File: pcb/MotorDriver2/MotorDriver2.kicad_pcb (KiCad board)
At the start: 4 copper layers, 112 parts, among them IC1 STM32C092RCT6, J1 GT-USB-7010ASV, J2 Conn_01x02, J3 Conn_01x02, J4 Conn_01x02, J5 Conn_01x02, Q1 IRLZ44NSTRLPBF, Q2 IRLZ44NSTRLPBF, Q3 IRLZ44NSTRLPBF, Q4 IRLZ44NSTRLPBF, Q5 IRLZ44NSTRLPBF, Q6 IRLZ44NSTRLPBF, Q7 IRLZ44NSTRLPBF, Q8 IRLZ44NSTRLPBF, SW1 K2-6639SP-C4SC-04, SW2 K2-6639SP-C4SC-04, SW3 K2-6639SP-C4SC-04, U1 NCP361SNT1G, U2 CH340X, U3 XIAO-ESP32-C5-DIP, U4 MCP2562FDT-H/SN, U5 MCP2562FDT-H/SN, U6 LM324DR, Y1 48 MHz, Y2 32.768 kHz

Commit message: Laying out PCB
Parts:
- removed H1, H2, H3: MountingHole, MountingHole:ToolingHole_1.152mm
- added C22: 100 nF, Capacitor_SMD:C_0603_1608Metric, F.Cu at (160.5, 145.5)
- added C23: 100 nF, Capacitor_SMD:C_0603_1608Metric, F.Cu at (160.5, 149.5)
- added C25: 4.7 uF, Capacitor_SMD:C_0603_1608Metric, F.Cu at (133.0, 115.5)
- added C26: 100 nF, Capacitor_SMD:C_0402_1005Metric, F.Cu at (133.5, 114.0)
- added D12: SM5819L2-TP, CapstoneFootprints:SDO_SM5819L2-TP_MCE, F.Cu at (181.5, 118.2)
- added D13: SM5819L2-TP, CapstoneFootprints:SDO_SM5819L2-TP_MCE, F.Cu at (181.5, 87.8)
- added D14: SM5819L2-TP, CapstoneFootprints:SDO_SM5819L2-TP_MCE, F.Cu at (122.2, 56.0)
- added IC2: CP2102N-A02-GQFN20R, CapstoneFootprints:CP2102NA02GQFN20, F.Cu at (135.5, 110.8)
- added R34: 10k, Resistor_SMD:R_0402_1005Metric, F.Cu at (139.5, 112.5)
- added R35: 1.5k, 1%, Resistor_SMD:R_0402_1005Metric, F.Cu at (126.0, 112.5)
- added R36: 1k, Resistor_SMD:R_0402_1005Metric, F.Cu at (136.0, 106.5)
- added R37: 1k, Resistor_SMD:R_0402_1005Metric, F.Cu at (132.5, 105.5)
- added R38: 10k, Resistor_SMD:R_0402_1005Metric, F.Cu at (218.5, 120.5)
- added R39: 1, Resistor_SMD:R_1206_3216Metric, F.Cu at (165.2, 101.5)
- added R40: 1, Resistor_SMD:R_1206_3216Metric, F.Cu at (165.2, 123.8)
- added R41: 10k, Resistor_SMD:R_0402_1005Metric, F.Cu at (236.0, 91.0)
- added R42: 10k, Resistor_SMD:R_0402_1005Metric, F.Cu at (236.0, 95.7)
- added R43: 1, Resistor_SMD:R_1206_3216Metric, F.Cu at (165.2, 83.8)
- added R44: 1, Resistor_SMD:R_1206_3216Metric, F.Cu at (122.5, 77.0)
- added TP1: TestPoint, TestPoint:TestPoint_Pad_1.0x1.0mm, B.Cu at (160.5, 91.5)
- added TP2: TestPoint, TestPoint:TestPoint_Pad_1.0x1.0mm, B.Cu at (160.5, 93.5)
- added TP3: TestPoint, TestPoint:TestPoint_Pad_1.0x1.0mm, B.Cu at (160.5, 95.5)
- C1, C2: value MAL214297108E3 -> Honor Elec RVT1H470M0607; footprint footprintLib:CAPAE680X800N -> CapstoneFootprints:CAPAE680X800N
- C10: value 100 nF -> Honor Elec RVT1H470M0607; footprint Capacitor_SMD:C_0402_1005Metric -> CapstoneFootprints:CAPAE680X800N
- C11: value 10 nF -> Honor Elec RVT1H470M0607; footprint Capacitor_SMD:C_0402_1005Metric -> CapstoneFootprints:CAPAE680X800N
- C12: value 100 nF -> 100 pF
- C20, C21: value MAL214297108E3 -> 100 nF; footprint footprintLib:CAPAE680X800N -> Capacitor_SMD:C_0603_1608Metric
- Conn2, Conn4, Conn5, Conn6, Conn8, R5, R7: moved to B.Cu
- D1: value SM5819L2-TP -> SP0502BAHTG; footprint footprintLib:SDO_SM5819L2-TP_MCE -> CapstoneFootprints:SOT95P237X112-3N
- D10, D9: value SM5819L2-TP -> LED; footprint footprintLib:SDO_SM5819L2-TP_MCE -> Diode_SMD:D_0402_1005Metric
- D11, D2, D3, D4, D8: footprint footprintLib:SDO_SM5819L2-TP_MCE -> CapstoneFootprints:SDO_SM5819L2-TP_MCE
- IC1: footprint footprintLib:QFP50P1200X1200X160-64N -> CapstoneFootprints:QFP50P1200X1200X160-64N
- J1: footprint footprintLib:USB4110-GF-A_GCT -> CapstoneFootprints:USB4110-GF-A_GCT
- Q1, Q3, Q5, Q6: footprint footprintLib:NMOSGDS_D2PAK_INF -> CapstoneFootprints:NMOSGDS_D2PAK_INF
- Q2, Q4, Q7, Q8: footprint footprintLib:NMOSGDS_D2PAK_INF -> CapstoneFootprints:NMOSGDS_D2PAK_INF; moved to B.Cu
- R13, R14: value 10k -> 20k
- R24, R25: value 1 -> 20k; footprint Resistor_SMD:R_1206_3216Metric -> Resistor_SMD:R_0402_1005Metric
- R26: value 10k -> 1k
- R27: value 10k -> 47.5k
- R28: value 1 -> 22.1k; footprint Resistor_SMD:R_1206_3216Metric -> Resistor_SMD:R_0402_1005Metric
- R29: value 1 -> 10k; footprint Resistor_SMD:R_1206_3216Metric -> Resistor_SMD:R_0402_1005Metric
- SW1, SW2, SW3: footprint footprintLib:K2-6639SP-C4SC-04 -> CapstoneFootprints:K2-6639SP-C4SC-04
- U1: footprint footprintLib:SOT95P275X110-5N -> CapstoneFootprints:SOT95P275X110-5N
- U2: value CH340X -> MAX40200AUK; footprint Package_SO:MSOP-10_3x3mm_P0.5mm -> Package_TO_SOT_SMD:SOT-23-5
- U3: footprint footprintLib:XIAO-ESP32-C5-DIP -> CapstoneFootprints:XIAO-ESP32-C5-DIP
- U6: footprint footprintLib:D14 -> CapstoneFootprints:D14
- VR1, VR2, VR3, VR4: footprint footprintLib:TS53YJ105MR10 -> CapstoneFootprints:TS53YJ105MR10
- Y1: footprint footprintLib:ECS-480-8-30-JGN-TR -> CapstoneFootprints:ECS-480-8-30-JGN-TR
- Y2: footprint footprintLib:MU00527-32.768K -> CapstoneFootprints:MU00527-32.768K
- moved Conn5 105.9 mm to (184.5, 96.0)
- moved Conn6 99.8 mm to (184.5, 86.5), turned to 180 degrees
- moved D11 84.8 mm to (181.5, 97.0), turned to -90 degrees
- moved Q7 84.8 mm to (173.0, 88.6), turned to 90 degrees
- moved Q6 84.3 mm to (173.1, 118.2), turned to -90 degrees
- moved R24 84.0 mm to (153.5, 142.0), turned to 180 degrees
- moved Q1 82.7 mm to (173.0, 96.5), turned to -90 degrees
- moved R25 77.5 mm to (153.8, 146.2), turned to 180 degrees
- moved C20 77.0 mm to (160.5, 137.0), turned to 180 degrees
- moved R14 74.2 mm to (154.0, 151.0), turned to 0 degrees
- moved C21 70.7 mm to (160.5, 141.0), turned to 180 degrees
- moved R13 66.6 mm to (165.4, 92.2), turned to 0 degrees
- moved R26 66.1 mm to (138.5, 114.5), turned to 0 degrees
- moved Conn7 66.0 mm to (129.2, 53.0), turned to 90 degrees
- moved D10 65.1 mm to (132.5, 107.0), turned to 180 degrees
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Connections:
- net /FDCAN/CAN_N renamed /digiControls/CAN_N
- net /FDCAN/CAN_P renamed /digiControls/CAN_P
- net /motorDriver_Pads12/Motor2- renamed /motors1/Motor1b-
- net /motorDriver_Pads12/Motor4- renamed /motors1/Motor2b-
- C10 pad 1: GND -> 5V
- C10 pad 2: 3V3 -> GND
- C11 pad 1: Net-(U2-V3) -> 5V
- C20 pad 1: 5V -> GND
- C20 pad 2: GND -> SensorAFilt
- C21 pad 1: 5V -> GND
- C21 pad 2: GND -> SensorBFilt
- Conn1 pad 2: /motorDriver_Pads12/Motor1- -> /motors1/Motor1a-
- Conn3 pad 2: /motorDriver_Pads12/Motor3- -> /motors1/Motor2a-
- Conn5 pad 2: /motorDriver_Pads34/Motor5- -> /motors2/Motor3a-
- Conn6 pad 2: /motorDriver_Pads34/Motor6- -> /motors2/Motor3b-
- Conn7 pad 2: /motorDriver_Pads34/Motor7- -> /motors2/Motor4a-
- Conn8 pad 2: /motorDriver_Pads34/Motor8- -> /motors2/Motor4b-
- D1 pad 1: 5V -> USB_D-
- D1 pad 2: /motorDriver_Pads34/Motor5- -> USB_D+
- D10 pad 1: 5V -> Net-(D10-K)
- D10 pad 2: /motorDriver_Pads34/Motor6- -> Net-(D10-A)
- D11 pad 2: /motorDriver_Pads34/Motor8- -> /motors2/Motor3a-
- D3 pad 2: /motorDriver_Pads12/Motor3- -> /motors1/Motor1a-
- D8 pad 2: /motorDriver_Pads12/Motor1- -> /motors2/Motor4a-
- D9 pad 1: 5V -> Net-(D9-K)
- D9 pad 2: /motorDriver_Pads34/Motor7- -> Net-(D9-A)
- IC1 pad 17: !CTS -> !CTS_STM
- IC1 pad 18: !RTS -> !RTS_STM
- IC1 pad 21: SensorAOut -> SensorAFilt
- IC1 pad 24: Motor4_PWM -> unconnected-(IC1-PA7-Pad24)
- IC1 pad 25: unconnected-(IC1-PC4-Pad25) -> Motor2a_PWM
- IC1 pad 26: unconnected-(IC1-PC5-Pad26) -> Motor2b_PWM
- IC1 pad 27: SensorDOut -> unconnected-(IC1-PB0-Pad27)
- IC1 pad 28: unconnected-(IC1-PB1-Pad28) -> SensorBFilt
- IC1 pad 30: unconnected-(IC1-PB10-Pad30) -> SensorCFilt
- IC1 pad 32: unconnected-(IC1-PB12-Pad32) -> SensorDFilt
- IC1 pad 38: unconnected-(IC1-PC6-Pad38) -> Motor3b_PWM
- IC1 pad 39: unconnected-(IC1-PC7-Pad39) -> Motor3a_PWM
- IC1 pad 40: unconnected-(IC1-PD8-Pad40) -> /stm32/SPI1_SCK
- IC1 pad 43: unconnected-(IC1-PA11_[PA9]-Pad43) -> /stm32/SPI1_MISO
- IC1 pad 44: unconnected-(IC1-PA12_[PA10]-Pad44) -> /stm32/SPI1_MOSI
- IC1 pad 47: Motor3_PWM -> Motor1a_PWM
- IC1 pad 57: Motor2_PWM -> Motor1b_PWM
- IC1 pad 58: Motor1_PWM -> unconnected-(IC1-PB4-Pad58)
- IC1 pad 60: unconnected-(IC1-PB6-Pad60) -> Motor4a_PWM
- IC1 pad 61: unconnected-(IC1-PB7-Pad61) -> Motor4b_PWM
- Q1 pad 1: Motor1_PWM -> Motor3a_PWM
- Q1 pad 2: /motorDriver_Pads34/Motor5- -> /motors2/Motor3a-
- Q2 pad 1: Motor2_PWM -> Motor1b_PWM
- Q3 pad 1: Motor3_PWM -> Motor1a_PWM
- Q3 pad 2: /motorDriver_Pads12/Motor3- -> /motors1/Motor1a-
- Q4 pad 1: Motor4_PWM -> Motor2b_PWM
- Q5 pad 1: Motor1_PWM -> Motor4a_PWM
- Q5 pad 2: /motorDriver_Pads12/Motor1- -> /motors2/Motor4a-
- Q6 pad 1: Motor3_PWM -> Motor2a_PWM
- Q6 pad 2: /motorDriver_Pads34/Motor7- -> /motors1/Motor2a-
- Q7 pad 1: Motor2_PWM -> Motor3b_PWM
- Q7 pad 2: /motorDriver_Pads34/Motor6- -> /motors2/Motor3b-
- Q8 pad 1: Motor4_PWM -> Motor4b_PWM
- Q8 pad 2: /motorDriver_Pads34/Motor8- -> /motors2/Motor4b-
- R1 pad 1: Motor1_PWM -> Motor4a_PWM
- R10 pad 1: !DTR -> (no net)
- R10 pad 2: BOOT -> (no net)
- R13 pad 1: Motor1_PWM -> SensorAOut
- R13 pad 2: GND -> SensorAFilt
- R14 pad 1: Motor3_PWM -> SensorBOut
- R14 pad 2: GND -> SensorBFilt
- R2 pad 1: Motor3_PWM -> Motor1a_PWM
- R24 pad 1: Net-(Q1-S) -> SensorDOut
- R24 pad 2: GND -> SensorDFilt
- R25 pad 1: Net-(Q6-S) -> SensorCOut
- R25 pad 2: GND -> SensorCFilt
- R26 pad 1: Motor2_PWM -> Net-(IC2-RSTB)
- R26 pad 2: GND -> 3V3
- R27 pad 1: Motor4_PWM -> Net-(IC2-VBUS)
- R28 pad 1: Net-(Q7-S) -> Net-(IC2-VBUS)
- R28 pad 2: GND -> 5V_USB
- R29 pad 1: Net-(Q8-S) -> Motor3a_PWM
- R5 pad 1: Motor2_PWM -> Motor1b_PWM
- R6 pad 1: Motor4_PWM -> Motor2b_PWM
- U2 pad 1: USB_D+ -> 5V
- U2 pad 2: USB_D- -> GND
- U2 pad 3: GND -> 5V
- U2 pad 4: !RTS -> unconnected-(U2-NC-Pad4)
- U2 pad 5: !CTS -> Net-(U2-OUT)
- U3 pad 14: 5V -> Net-(U2-OUT)
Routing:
- net 5V: track 259.9 -> 63.8 mm
- net Motor1_PWM: track 34.2 -> 0.00 mm
- net Motor4b_PWM: track 0.00 -> 33.2 mm, vias 0 -> 1
- net Motor4a_PWM: track 0.00 -> 29.7 mm
- net Motor4_PWM: track 26.1 -> 0.00 mm, vias 2 -> 0
- net Motor2_PWM: track 22.2 -> 0.00 mm, vias 2 -> 0
- net 3V3: track 42.3 -> 24.2 mm, vias 9 -> 4
- net !RTS: track 17.8 -> 0.00 mm, vias 2 -> 0
- net !CTS: track 16.1 -> 0.00 mm, vias 2 -> 0
- net /motorDriver_Pads34/Motor7-: track 15.1 -> 0.00 mm
- net BOOT: track 16.9 -> 1.97 mm
- net USER_BTN: track 19.1 -> 4.89 mm
- net SensorBIn: track 6.87 -> 20.9 mm
- net SensorAIn: track 15.5 -> 29.5 mm, vias 0 -> 2
- net NRST: track 24.9 -> 10.9 mm
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- removed copper zone on B.Cu, net GND
- removed copper zone on F.Cu, net GND
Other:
- board outline added: 76.5 x 82 mm
- board text added: "Emma Ouyang, Emma Steinberg Ashley Luo, Siyang Sun"
- board text removed: "Emma Ouyang, Emma Steinberg, Ashley Luo, Siyang Sun"
- board text removed: "WARNING: DO NOT USE ESP USB IF BATTERY IS ON"

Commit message: Finished pcb layout
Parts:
- removed D1: SP0502BAHTG, CapstoneFootprints:SOT95P237X112-3N
- removed R10: DNP, Resistor_SMD:R_0402_1005Metric
- added G***: LOGO, LOGO, F.Cu at (117.0, 127.0)
- added U7: USBLC6-2SC6, Package_TO_SOT_SMD:SOT-23-6, F.Cu at (128.5, 111.0)
- C20, C21, C22, C23: footprint Capacitor_SMD:C_0603_1608Metric -> Capacitor_SMD:C_0402_1005Metric
- J1: value GT-USB-7010ASV -> USB4110-GF-A
- R5, R7: moved to F.Cu
- moved R42 111.6 mm to (126.0, 77.0), turned to -90 degrees
- moved R41 71.0 mm to (165.0, 92.5), turned to 180 degrees
- moved R38 56.7 mm to (162.0, 116.0), turned to -90 degrees
- moved C23 46.3 mm to (152.0, 104.0)
- moved R14 44.7 mm to (149.8, 106.5)
- moved C22 40.9 mm to (155.0, 105.0)
- moved R25 40.3 mm to (153.0, 106.0), turned to 90 degrees
- moved C21 36.7 mm to (151.3, 105.5)
- moved R24 35.5 mm to (154.5, 106.5), turned to 90 degrees
- moved C20 33.6 mm to (148.8, 105.5)
- moved R13 22.7 mm to (147.8, 106.5), turned to 180 degrees
- moved R11 10.6 mm to (126.0, 97.0), turned to -90 degrees
- moved R2 10.3 mm to (162.0, 74.5), turned to 90 degrees
- moved D7 8.73 mm to (124.5, 97.0), turned to -90 degrees
- moved G*** 8.06 mm to (124.0, 127.0)
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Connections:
- IC1 pad 22: unconnected-(IC1-PA5-Pad22) -> SensorBFilt
- IC1 pad 23: unconnected-(IC1-PA6-Pad23) -> SensorCFilt
- IC1 pad 24: unconnected-(IC1-PA7-Pad24) -> SensorDFilt
- IC1 pad 28: SensorBFilt -> unconnected-(IC1-PB1-Pad28)
- IC1 pad 30: SensorCFilt -> unconnected-(IC1-PB10-Pad30)
- IC1 pad 32: SensorDFilt -> unconnected-(IC1-PB12-Pad32)
- R28 pad 2: 5V_USB -> VBUS
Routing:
- net GND: track 18.1 -> 99.3 mm, vias 11 -> 60
- net 5V: track 63.8 -> 102.9 mm, vias 5 -> 6
- net BOOT: track 1.97 -> 38.2 mm, vias 0 -> 2
- net 3V3: track 24.2 -> 60.2 mm, vias 4 -> 16
- net VBUS: track 9.72 -> 34.7 mm, vias 0 -> 2
- net Motor1b_PWM: track 2.72 -> 27.3 mm, vias 1 -> 2
- net Motor2a_PWM: track 0.00 -> 23.4 mm
- net !DTR: track 19.0 -> 0.00 mm, vias 2 -> 0
- net Motor3b_PWM: track 0.00 -> 18.2 mm, vias 0 -> 1
- net Motor1a_PWM: track 3.68 -> 21.3 mm
- net Motor2b_PWM: track 3.43 -> 19.3 mm
- net !CTS_STM: track 4.31 -> 17.7 mm, vias 1 -> 0
- net !RTS_STM: track 4.76 -> 18.0 mm, vias 1 -> 0
- net /motors1/Motor1a-: track 0.00 -> 10.4 mm
- net SensorCOut: track 12.9 -> 22.5 mm, vias 0 -> 2
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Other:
- board size 76.5 x 82 mm -> 77 x 82 mm
- board text added: "82 x 77 mm"
- board text added: "Motor1a"
- board text added: "Motor1b"
- board text added: "Motor2a"
- board text added: "Motor2b"
- board text added: "Motor3a"
- board text added: "Motor3b"
- board text added: "Motor4a"
- board text added: "Motor4b"
- board text added: "SPI1_MISO"
- board text added: "SPI1_MOSI"
- board text added: "SPI1_SCK"
- board text removed: "72 x 76 mm"
- board text removed: "Motor1"
- board text removed: "Motor2"
- board text removed: "Motor3"
- board text removed: "Motor4"

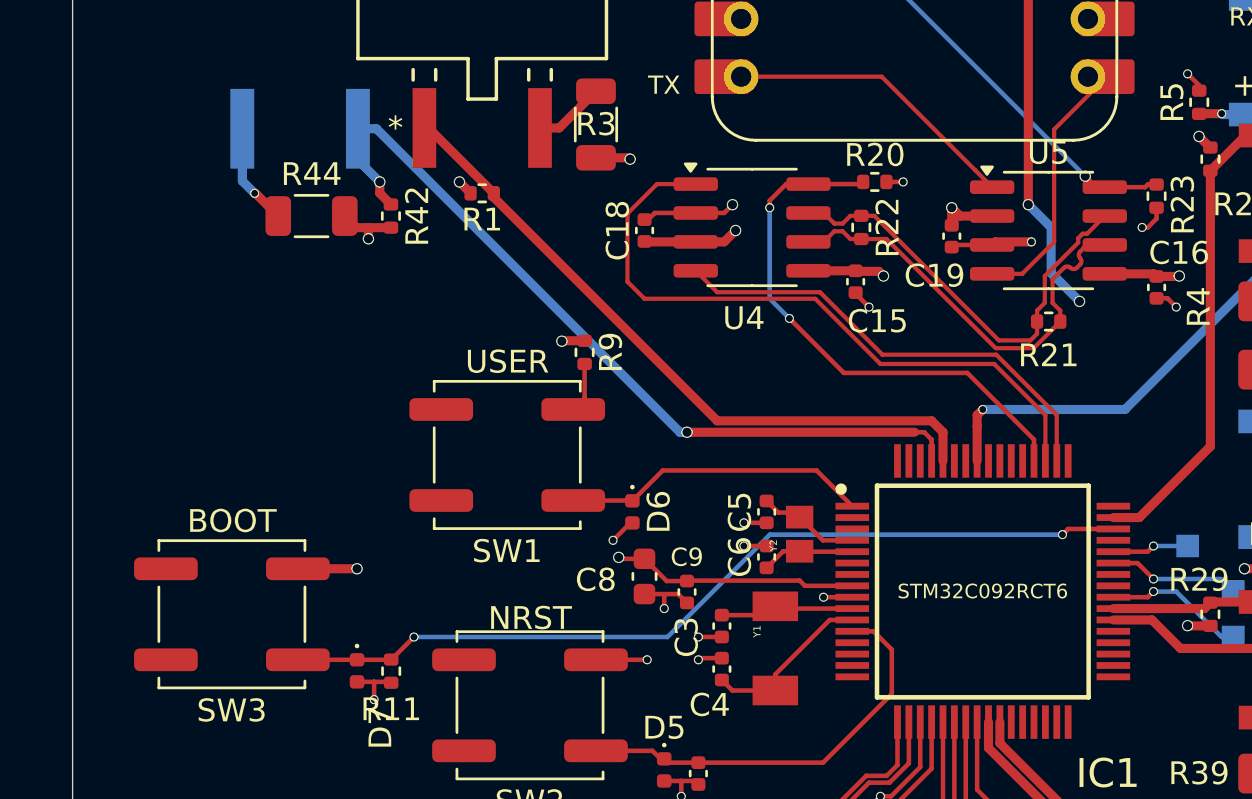
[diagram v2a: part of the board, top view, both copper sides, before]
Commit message: Added STLink Connector
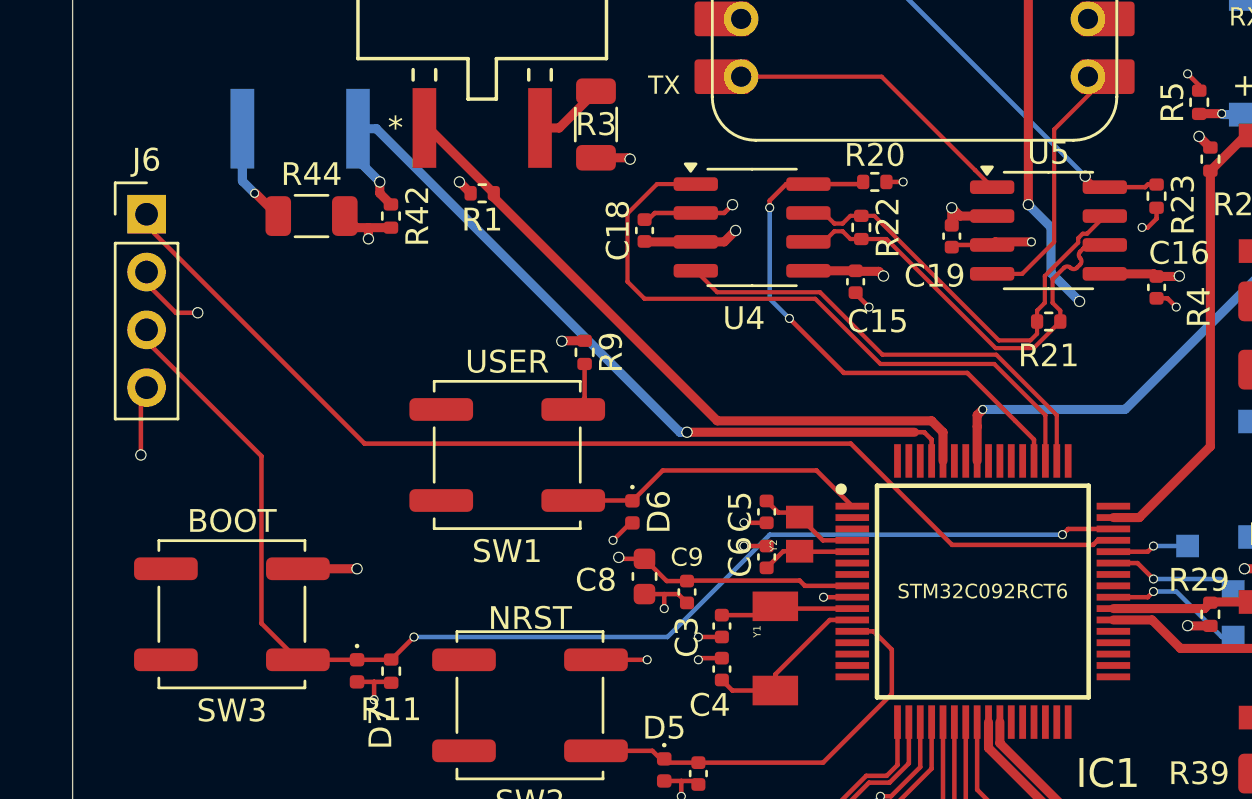
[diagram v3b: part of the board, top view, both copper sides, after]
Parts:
- added J6: Conn_01x04, Connector_PinHeader_2.54mm:PinHeader_1x04_P2.54mm_Vertical, F.Cu at (115.2, 76.9)
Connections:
- IC1 pad 45: unconnected-(IC1-PA13-Pad45) -> SWDIO
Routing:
- net SWDIO: track 0.00 -> 49.1 mm
- net BOOT: track 38.2 -> 55.7 mm
- net GND: track 99.3 -> 102.8 mm, vias 60 -> 61
- net 3V3: track 60.2 -> 63.2 mm, vias 16 -> 17

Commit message: Removed can transceivers, replaced with spi
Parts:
- removed C15, C16, C18, C19: 100 nF, Capacitor_SMD:C_0402_1005Metric
- removed R20, R23: 10k, Resistor_SMD:R_0402_1005Metric
- removed R21, R22: 120, Resistor_SMD:R_0402_1005Metric
- removed U4, U5: MCP2562FDT-H/SN, Package_SO:SOIC-8_3.9x4.9mm_P1.27mm
- added H1: MountingHole, MountingHole:ToolingHole_1.152mm, F.Cu at (115.0, 124.0)
- added H2: MountingHole, MountingHole:ToolingHole_1.152mm, F.Cu at (186.0, 124.0)
- added H3: MountingHole, MountingHole:ToolingHole_1.152mm, F.Cu at (116.0, 55.0)
- TP1, TP2, TP3: moved to F.Cu
- moved TP2 14.8 mm to (153.8, 82.0)
- moved TP1 14.7 mm to (152.5, 79.5)
- moved TP3 13.6 mm to (154.8, 84.8), turned to 180 degrees
- moved VBAT1 1.00 mm to (184.5, 55.5)
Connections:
- IC1 pad 40: /stm32/SPI1_SCK -> unconnected-(IC1-PD8-Pad40)
- IC1 pad 42: unconnected-(IC1-PA10-Pad42) -> SPI1_CS
- IC1 pad 43: /stm32/SPI1_MISO -> unconnected-(IC1-PA11_[PA9]-Pad43)
- IC1 pad 44: /stm32/SPI1_MOSI -> unconnected-(IC1-PA12_[PA10]-Pad44)
- IC1 pad 50: FDCAN_RX_STM -> unconnected-(IC1-PD0-Pad50)
- IC1 pad 51: FDCAN_TX_STM -> SPI2_SCK
- IC1 pad 52: FDCAN_STBY_STM -> unconnected-(IC1-PD2-Pad52)
- IC1 pad 53: unconnected-(IC1-PD3-Pad53) -> SPI2_MISO
- IC1 pad 54: unconnected-(IC1-PD4-Pad54) -> SPI2_MOSI
- IC1 pad 59: unconnected-(IC1-PB5-Pad59) -> CS
- TP1 pad 1: /stm32/SPI1_MOSI -> SPI2_MOSI
- TP2 pad 1: /stm32/SPI1_MISO -> SPI2_MISO
- TP3 pad 1: /stm32/SPI1_SCK -> SPI2_SCK
- U3 pad 1: FDCAN_STBY_ESP -> unconnected-(U3-GPIO2_A0_D0-Pad1)_1
- U3 pad 10: unconnected-(U3-GPIO9_D9_MISO-Pad10)_1 -> SPI2_MISO
- U3 pad 11: unconnected-(U3-GPIO10_D10_MOSI-Pad11) -> SPI2_MOSI
- U3 pad 3: unconnected-(U3-GPIO4_A2_D2-Pad3)_1 -> CS
- U3 pad 7: FDCAN_TX_ESP -> unconnected-(U3-GPIO21_D6_TX-Pad7)_1
- U3 pad 8: FDCAN_RX_ESP -> unconnected-(U3-GPIO20_D7_RX-Pad8)
- U3 pad 9: unconnected-(U3-GPIO8_D8_SCK-Pad9)_1 -> SPI2_SCK
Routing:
- net 5V: track 102.9 -> 52.5 mm, vias 6 -> 4
- net CS: track 0.00 -> 30.9 mm
- net FDCAN_TX_STM: track 29.5 -> 0.00 mm
- net FDCAN_STBY_ESP: track 29.3 -> 0.00 mm, vias 1 -> 0
- net SPI2_MOSI: track 0.00 -> 26.5 mm
- net FDCAN_STBY_STM: track 23.9 -> 0.00 mm, vias 2 -> 0
- net SPI2_MISO: track 0.00 -> 23.7 mm
- net FDCAN_RX_STM: track 20.5 -> 0.00 mm
- net SPI2_SCK: track 0.00 -> 20.2 mm
- net /digiControls/CAN_P: track 19.3 -> 0.00 mm
- net /digiControls/CAN_N: track 19.2 -> 0.00 mm
- net FDCAN_TX_ESP: track 13.5 -> 0.00 mm
- net FDCAN_RX_ESP: track 11.5 -> 0.00 mm
- net GND: track 102.8 -> 92.7 mm, vias 61 -> 55
- net /stm32/SPI1_SCK: track 6.19 -> 0.00 mm, vias 1 -> 0
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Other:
- board text added: "CS"
- board text added: "MISO"
- board text added: "MOSI"
- board text added: "SCK"
- board text removed: "FDCAN STBY"
- board text removed: "TX"
